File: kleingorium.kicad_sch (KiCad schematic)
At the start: 37 parts, among them J1 4017 Pins, J10 VCC, J11 GND, J12 4046 Comp In, J13 Select, J14 Input, J15 4046 SigIn, J16 4046 Comp, J17 Output, J18 4046 Comp In, J19 4046 Out, J2 4040 Output, J20 4040 Input, J21 4040 Output, J22 4017 Pins, J23 VCC, J24 GND, J3 4040 Input, J4 4046 Out, J5 4046 Comp, J6 Select, J7 Output, J8 Input, J9 4046 SigIn, Q1 2N3904, Q2 2N3904, SW1 4017 Feedback, SW2 4046 CompIn, SW3 Chain, SW4 4017 Feedback, SW5 4046 CompIn

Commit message: remove pull down resistor, change pull up from 10k to 2.2k
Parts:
- removed R15, R16: 10k, Resistor_THT:R_Axial_DIN0207_L6.3mm_D2.5mm_P10.16mm_Horizontal, symbol Device:R_Small
- R11, R14: value 10k -> 2.2k
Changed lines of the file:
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@@
 	)
 	(junction
-		(at 83.82 245.11)
-		(diameter 0)
-		(color 0 0 0 0)
-	)
-	(junction
-		(at 73.66 256.54)
-		(diameter 0)
-		(color 0 0 0 0)
-	)
-	(junction
 		(at 91.44 116.84)
 		(diameter 0)
@@
 	)
 	(junction
-		(at 73.66 36.83)
-		(diameter 0)
-		(color 0 0 0 0)
-	)
-	(junction
 		(at 184.15 69.85)
 		(diameter 0)
@@
 	)
 	(junction
-		(at 82.55 48.26)
-		(diameter 0)
-		(color 0 0 0 0)
-	)
-	(junction
 		(at 254 45.72)
 		(diameter 0)
@@
 	(wire
 		(pts
-			(xy 73.66 48.26) (xy 82.55 48.26)
-		)
-		(stroke
-			(width 0)
-			(type default)
-		)
-	)
-	(wire
-		(pts
 			(xy 194.31 54.61) (xy 194.31 199.39)
 		)
@@
 	(wire
 		(pts
-			(xy 82.55 48.26) (xy 163.83 48.26)
+			(xy 73.66 48.26) (xy 163.83 48.26)
 		)
 		(stroke
@@
 	(wire
 		(pts
-			(xy 73.66 36.83) (xy 82.55 36.83)
-		)
-		(stroke
-			(width 0)
-			(type default)
-		)
-	)
-	(wire
-		(pts
 			(xy 254 38.1) (xy 266.7 38.1)
 		)
@@
 	(wire
 		(pts
-			(xy 82.55 44.45) (xy 82.55 48.26)
-		)
-		(stroke
-			(width 0)
-			(type default)
-		)
-	)
-	(wire
-		(pts
 			(xy 264.16 196.85) (xy 276.86 196.85)
 		)
@@
 	(wire
 		(pts
-			(xy 82.55 39.37) (xy 82.55 36.83)
-		)
-		(stroke
-			(width 0)
-			(type default)
-		)
-	)
-	(wire
-		(pts
 			(xy 251.46 107.95) (xy 264.16 107.95)
 		)
@@
 	(wire
 		(pts
-			(xy 73.66 245.11) (xy 83.82 245.11)
+			(xy 73.66 245.11) (xy 140.97 245.11)
 		)
 		(stroke
@@
 	(wire
 		(pts
-			(xy 83.82 245.11) (xy 140.97 245.11)
-		)
-		(stroke
-			(width 0)
-			(type default)
-		)
-	)
-	(wire
-		(pts
 			(xy 74.93 116.84) (xy 74.93 102.87)
 		)
@@
 	(wire
 		(pts
-			(xy 83.82 256.54) (xy 73.66 256.54)
-		)
-		(stroke
-			(width 0)
-			(type default)
-		)
-	)
-	(wire
-		(pts
 			(xy 74.93 175.26) (xy 74.93 189.23)
 		)
@@
 	(wire
 		(pts
-			(xy 83.82 245.11) (xy 83.82 250.19)
-		)
-		(stroke
-			(width 0)
-			(type default)
-		)
-	)
-	(wire
-		(pts
 			(xy 251.46 196.85) (xy 264.16 196.85)
 		)
@@
 	(wire
 		(pts
-			(xy 83.82 256.54) (xy 83.82 255.27)
-		)
-		(stroke
-			(width 0)
-			(type default)
-		)
-	)
-	(wire
-		(pts
 			(xy 264.16 82.55) (xy 276.86 82.55)
 		)
@@
 	)
 	(symbol
-		(lib_id "Device:R_Small")
-		(at 82.55 41.91 0)
-		(unit 1)
-		(exclude_from_sim no)
-		(in_bom yes)
-		(on_board yes)
-		(dnp no)
-		(fields_autoplaced yes)
-		(property "Reference" "R16"
-			(at 85.09 40.6399 0)
-			(effects
-				(font
-					(size 1.016 1.016)
-				)
-				(justify left)
-			)
-		)
-		(property "Value" "10k"
-			(at 85.09 43.1799 0)
-			(effects
-				(font
-					(size 1.27 1.27)
-				)
-				(justify left)
-			)
-		)
-		(property "Footprint" "Resistor_THT:R_Axial_DIN0207_L6.3mm_D2.5mm_P10.16mm_Horizontal"
-			(at 82.55 41.91 0)
-			(effects
-				(font
-					(size 1.27 1.27)
-				)
-				(hide yes)
-			)
-		)
-		(property "Datasheet" "~"
-			(at 82.55 41.91 0)
-			(effects
-				(font
-					(size 1.27 1.27)
-				)
-				(hide yes)
-			)
-		)
-		(property "Description" "Resistor, small symbol"
-			(at 82.55 41.91 0)
-			(effects
-				(font
-					(size 1.27 1.27)
-				)
-				(hide yes)
-			)
-		)
-		(pin "2"
-		)
-		(pin "1"
-		)
-		(instances
-			(project "kleingorium"
-				(path "/01c1f2c1-4d06-4880-847a-9ab55552e3fd"
-					(reference "R16")
-					(unit 1)
-				)
-			)
-		)
-	)
-	(symbol
 		(lib_id "Switch:SW_SPDT")
 		(at 107.95 252.73 270)
@@
 			)
 		)
-		(property "Value" "10k"
+		(property "Value" "2.2k"
 			(at 76.2 242.5699 0)
 			(effects
@@
 			)
 		)
-		(property "Value" "10k"
+		(property "Value" "2.2k"
 			(at 76.2 49.5301 0)
 			(effects
@@
 					(unit 1)
 				)
-			)
-		)
-	)
-	(symbol
-		(lib_id "Device:R_Small")
-		(at 83.82 252.73 0)
-		(unit 1)
-		(exclude_from_sim no)
-		(in_bom yes)
-		(on_board yes)
-		(dnp no)
-		(fields_autoplaced yes)
-		(property "Reference" "R15"
-			(at 86.36 251.4599 0)
-			(effects
-				(font
-					(size 1.016 1.016)
-				)
-				(justify left)
-			)
-		)
-		(property "Value" "10k"
-			(at 86.36 253.9999 0)
-			(effects
-				(font
-					(size 1.27 1.27)
-				)
-				(justify left)
-			)
-		)
-		(property "Footprint" "Resistor_THT:R_Axial_DIN0207_L6.3mm_D2.5mm_P10.16mm_Horizontal"
-			(at 83.82 252.73 0)
-			(effects
-				(font
-					(size 1.27 1.27)
-				)
-				(hide yes)
-			)
-		)
-		(property "Datasheet" "~"
-			(at 83.82 252.73 0)
-			(effects
-				(font
-					(size 1.27 1.27)
-				)
-				(hide yes)
-			)
-		)
-		(property "Description" "Resistor, small symbol"
-			(at 83.82 252.73 0)
-			(effects
-				(font
-					(size 1.27 1.27)
-				)
-				(hide yes)
-			)
-		)
-		(pin "2"
-		)
-		(pin "1"
-		)
-		(instances
-			(project "kleingorium"
-				(path "/01c1f2c1-4d06-4880-847a-9ab55552e3fd"
-					(reference "R15")
-					(unit 1)
-				)

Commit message: add Select transistor
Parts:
- added Q3, Q4: 2N3904, Package_TO_SOT_THT:TO-92_Inline_Wide, symbol Transistor_BJT:2N3904
- added R15, R16: 100k, Resistor_THT:R_Axial_DIN0207_L6.3mm_D2.5mm_P2.54mm_Vertical, symbol Device:R_Small
- added RV1, RV2, RV3, RV4: 1K, Potentiometer_THT:Potentiometer_Bourns_3296W_Vertical, symbol Device:R_Potentiometer_Trim
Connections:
- net 4017 2/Q0: now also RV2.1, RV2.2
- net 4017 2/Reset: now also RV4.1, RV4.2
- net 4017/Q0: now also RV1.1, RV1.2
- net 4017/Reset: now also RV3.1, RV3.2
- net 4053 2/Select: no longer J13.1 (Pin_1), J13.2 (Pin_2)
- net 4053/Select: no longer J6.1 (Pin_1), J6.2 (Pin_2)
- net GND: now also R15.1, R16.1
- net VCC: now also Q3.3 (C), Q4.3 (C), RV1.3, RV2.3, RV3.3, RV4.3
- new net: J6.1 (Pin_1), J6.2 (Pin_2), Q3.2 (B)
- new net: Q3.1 (E), R15.2
- new net: Q4.1 (E), R16.2
- new net: J13.1 (Pin_1), J13.2 (Pin_2), Q4.2 (B)
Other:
- added sheet Feedback design (feedback_design.kicad_sch)
- moved on the sheet: J13, J4, J5, J6, J9, SW2

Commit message: add pull-down to A1, remove Q0 pull up
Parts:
- added Q5, Q6: 2N3904, Package_TO_SOT_THT:TO-92_Inline_Wide, symbol Transistor_BJT:2N3904
- added R17, R18: 100k, Resistor_THT:R_Axial_DIN0207_L6.3mm_D2.5mm_P2.54mm_Vertical, symbol Device:R_Small
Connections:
- net 4017 2/Q0: no longer RV2.1, RV2.2
- net 4017/Q0: no longer RV1.1, RV1.2
- net 4046 2/SigIn: now also RV2.1, RV2.2
- net 4046/SigIn: now also RV1.1, RV1.2
- net 4053 2/A: now also Q6.1 (E), R18.2; no longer J14.1 (Pin_1), J14.2 (Pin_2), SW3.1 (A)
- net 4053/A: now also Q5.1 (E), R17.2; no longer J8.1 (Pin_1), J8.2 (Pin_2)
- net GND: now also RV1.3, RV2.3, R17.1, R18.1
- net VCC: now also Q5.3 (C), Q6.3 (C); no longer RV1.3, RV2.3
- net power/gnd: now also J24.1 (Pin_1), J24.2 (Pin_2)
- net power/vcc: now also J23.1 (Pin_1), J23.2 (Pin_2)
- new net: J8.1 (Pin_1), J8.2 (Pin_2), Q5.2 (B)
- new net: J14.1 (Pin_1), J14.2 (Pin_2), Q6.2 (B), SW3.1 (A)
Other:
- removed sheet Feedback design
- moved on the sheet: J12, J14, J18, J8, RV1, RV2

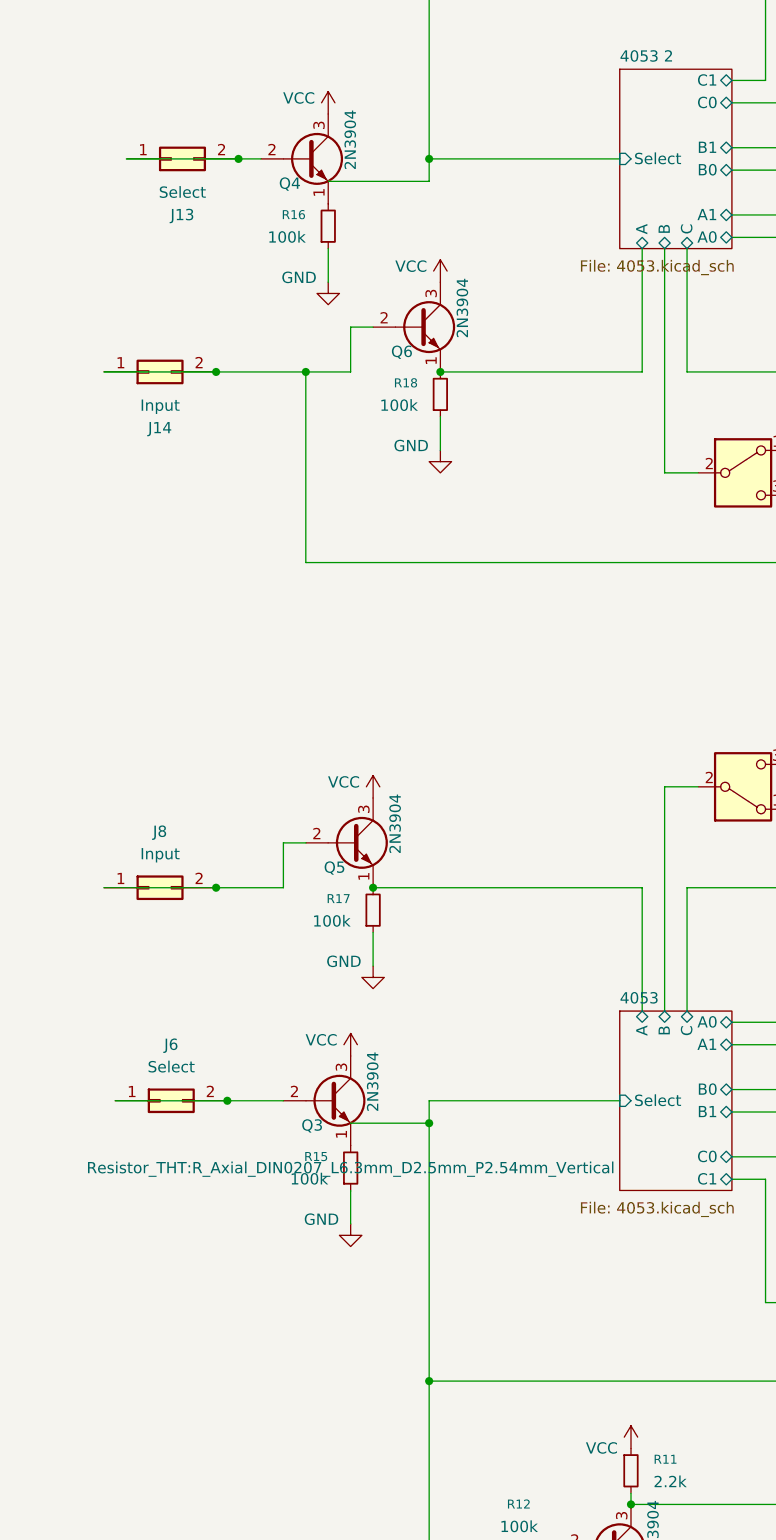
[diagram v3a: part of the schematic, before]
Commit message: fix transistor circuit issue
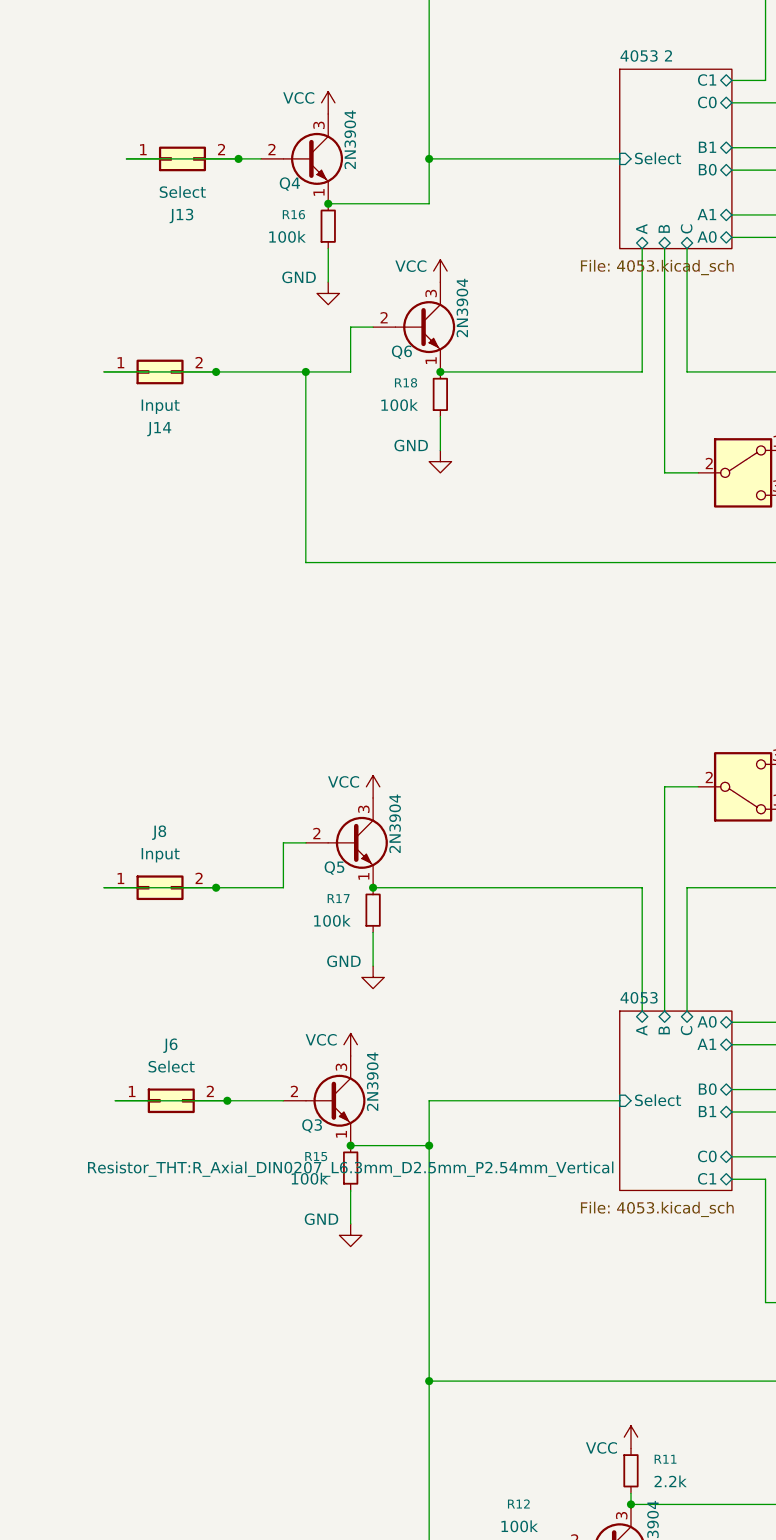
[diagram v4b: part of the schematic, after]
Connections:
- net 4053 2/Select: now also Q4.1 (E), R16.2
- net 4053/Select: now also Q3.1 (E), R15.2
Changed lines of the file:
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@@
 	)
 	(junction
+		(at 41.91 204.47)
+		(diameter 0)
+		(color 0 0 0 0)
+	)
+	(junction
 		(at 154.94 200.66)
 		(diameter 0)
@@
 	)
 	(junction
+		(at 50.8 204.47)
+		(diameter 0)
+		(color 0 0 0 0)
+	)
+	(junction
 		(at 114.3 271.78)
 		(diameter 0)
@@
 	)
 	(junction
-		(at 50.8 201.93)
-		(diameter 0)
-		(color 0 0 0 0)
-	)
-	(junction
 		(at 266.7 236.22)
 		(diameter 0)
@@
 	)
 	(junction
+		(at 39.37 97.79)
+		(diameter 0)
+		(color 0 0 0 0)
+	)
+	(junction
 		(at 50.8 92.71)
 		(diameter 0)
@@
 	(wire
 		(pts
-			(xy 50.8 201.93) (xy 50.8 231.14)
+			(xy 50.8 199.39) (xy 50.8 204.47)
 		)
 		(stroke
@@
 	(wire
 		(pts
-			(xy 41.91 201.93) (xy 50.8 201.93)
+			(xy 41.91 204.47) (xy 50.8 204.47)
 		)
 		(stroke
@@
 	(wire
 		(pts
-			(xy 39.37 95.25) (xy 50.8 95.25)
+			(xy 39.37 97.79) (xy 50.8 97.79)
 		)
 		(stroke
@@
 	(wire
 		(pts
+			(xy 50.8 204.47) (xy 50.8 231.14)
+		)
+		(stroke
+			(width 0)
+			(type default)
+		)
+	)
+	(wire
+		(pts
 			(xy 254 238.76) (xy 266.7 238.76)
 		)
@@
 	(wire
 		(pts
-			(xy 50.8 199.39) (xy 50.8 201.93)
-		)
-		(stroke
-			(width 0)
-			(type default)
-		)
-	)
-	(wire
-		(pts
 			(xy 294.64 210.82) (xy 294.64 212.09)
 		)
@@
 	(wire
 		(pts
-			(xy 50.8 95.25) (xy 50.8 92.71)
+			(xy 50.8 97.79) (xy 50.8 92.71)
 		)
 		(stroke

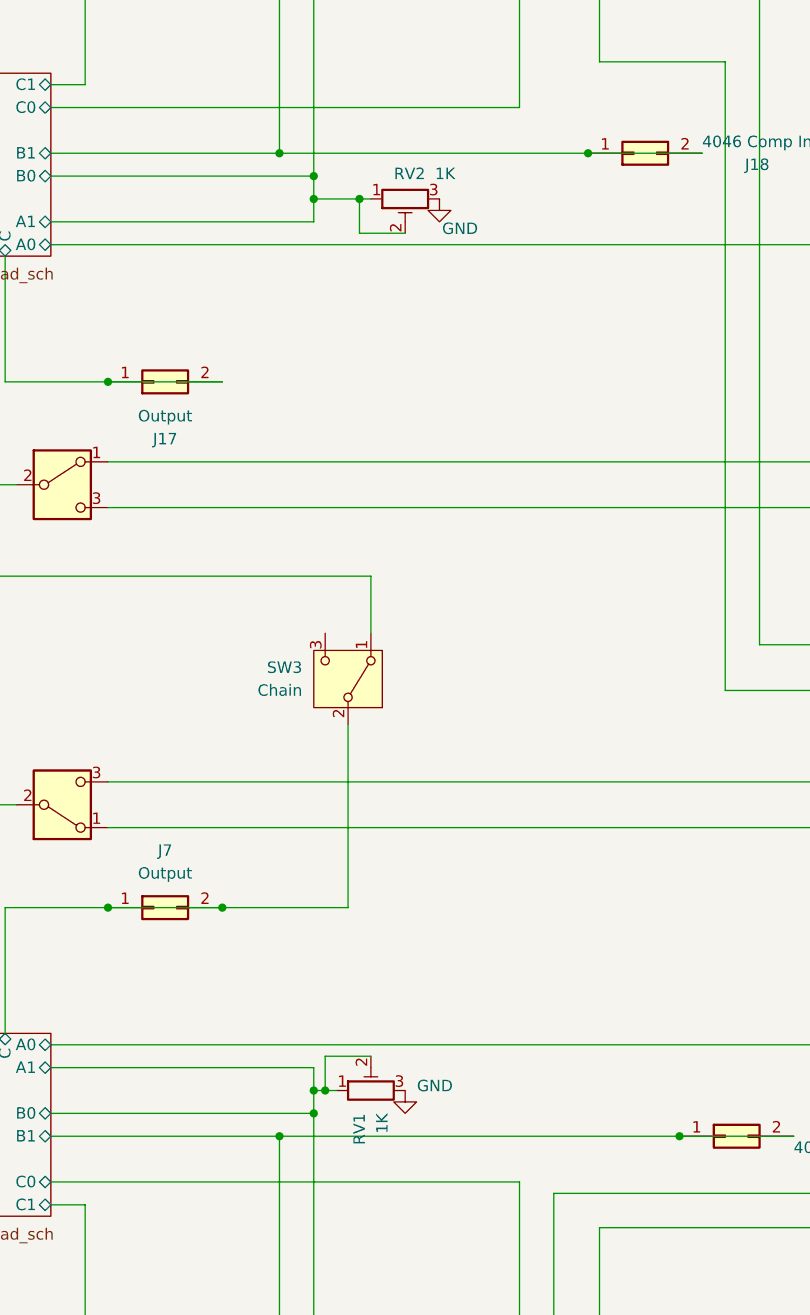
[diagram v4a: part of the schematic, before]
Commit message: remove RV3,4 and change RV1,2 to 2k
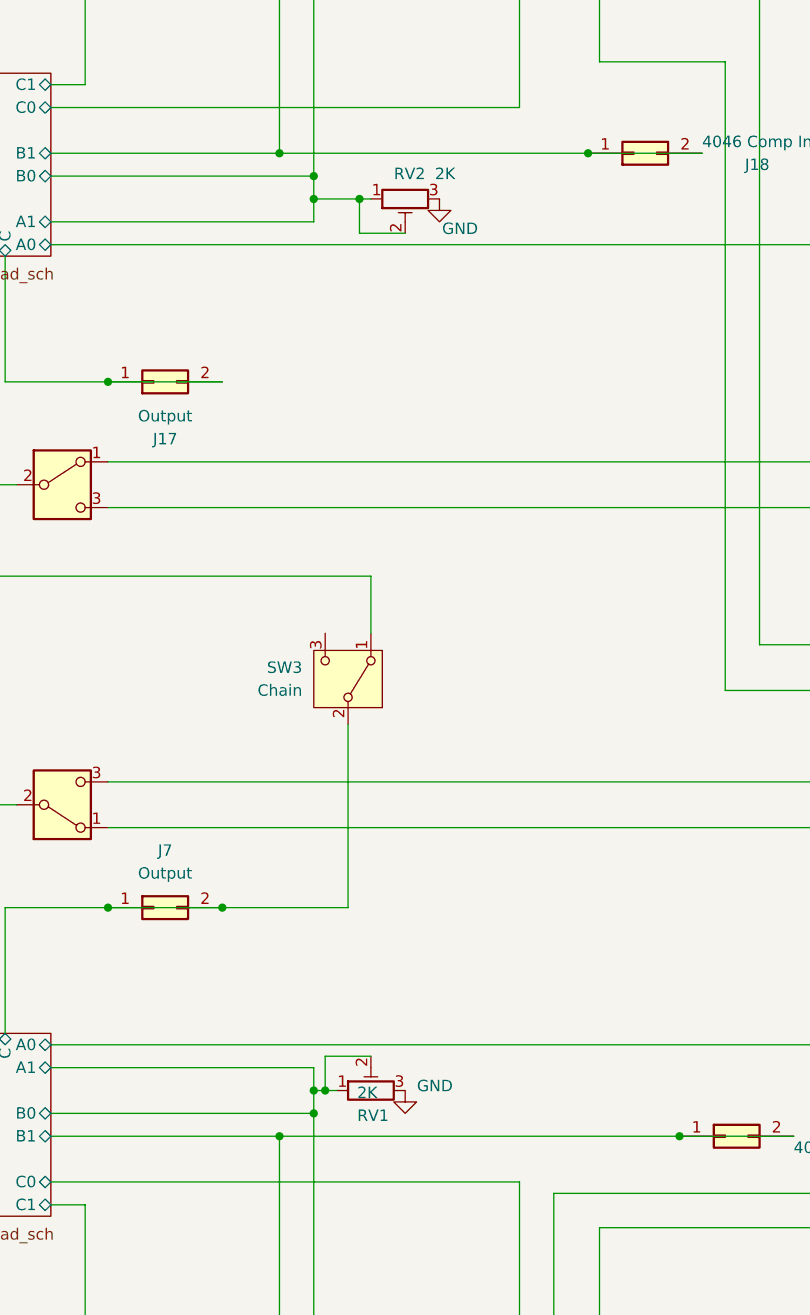
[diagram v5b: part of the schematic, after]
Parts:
- RV1, RV2: value 1K -> 2K
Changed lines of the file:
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@@
 			)
 		)
-		(property "Value" "1K"
+		(property "Value" "2K"
 			(at 127.762 93.726 90)
 			(effects
@@
 		(dnp no)
 		(property "Reference" "RV1"
-			(at 119.3799 198.12 0)
+			(at 119.126 198.374 90)
 			(effects
 				(font
@@
 			)
 		)
-		(property "Value" "1K"
-			(at 121.9199 198.12 0)
-			(effects
-				(font
+		(property "Value" "2K"
+			(at 119.126 195.834 90)
+			(effects
+				(font
